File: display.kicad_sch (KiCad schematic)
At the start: 29 parts, among them Q1 HL2300, Q2 HL2300, Q3 HL2300, Q4 HL2300, Q5 HL2300, Q6 HL2300, Q7 HL2300, Q8 HL2300, U2 GS3911AG

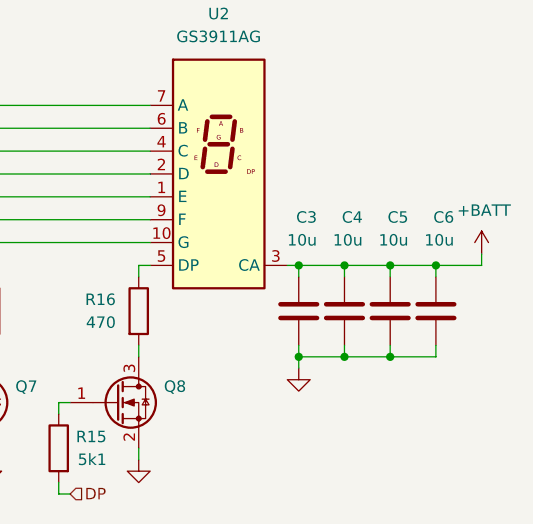
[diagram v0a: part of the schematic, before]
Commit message: schem: remove display extra decoupling caps
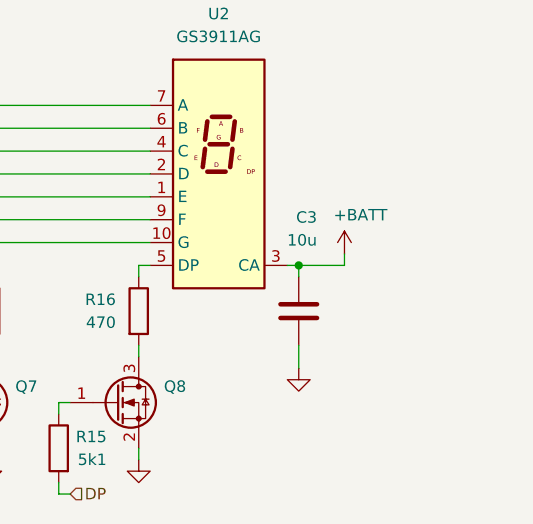
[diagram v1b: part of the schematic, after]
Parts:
- removed C4, C5, C6: 10u, Capacitor_SMD:C_0805_2012Metric, symbol Device:C

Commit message: pcb: add segment displays layout
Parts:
- added C4: 10u, Capacitor_SMD:C_0805_2012Metric, symbol Device:C
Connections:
- net +BATT: now also C4.1
- net GND: now also C4.2
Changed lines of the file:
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@@
 	)
 	(junction
+		(at 215.9 99.06)
+		(diameter 0)
+		(color 0 0 0 0)
+	)
+	(junction
 		(at 215.9 88.9)
 		(diameter 0)
 		(color 0 0 0 0)
 	)
+	(junction
+		(at 220.98 88.9)
+		(diameter 0)
+		(color 0 0 0 0)
+	)
 	(wire
 		(pts
@@
 	(wire
 		(pts
+			(xy 220.98 88.9) (xy 224.79 88.9)
+		)
+		(stroke
+			(width 0)
+			(type default)
+		)
+	)
+	(wire
+		(pts
 			(xy 199.39 83.82) (xy 165.1 83.82)
 		)
@@
 	(wire
 		(pts
+			(xy 220.98 88.9) (xy 220.98 90.17)
+		)
+		(stroke
+			(width 0)
+			(type default)
+		)
+	)
+	(wire
+		(pts
 			(xy 198.12 88.9) (xy 198.12 90.17)
 		)
@@
 	(wire
 		(pts
+			(xy 215.9 99.06) (xy 215.9 100.33)
+		)
+		(stroke
+			(width 0)
+			(type default)
+		)
+	)
+	(wire
+		(pts
+			(xy 220.98 99.06) (xy 220.98 97.79)
+		)
+		(stroke
+			(width 0)
+			(type default)
+		)
+	)
+	(wire
+		(pts
 			(xy 124.46 114.3) (xy 123.19 114.3)
 		)
@@
 	(wire
 		(pts
-			(xy 220.98 88.9) (xy 220.98 87.63)
+			(xy 224.79 88.9) (xy 224.79 87.63)
 		)
 		(stroke
@@
 	(wire
 		(pts
-			(xy 215.9 97.79) (xy 215.9 100.33)
+			(xy 215.9 97.79) (xy 215.9 99.06)
 		)
 		(stroke
@@
 	(wire
 		(pts
+			(xy 215.9 99.06) (xy 220.98 99.06)
+		)
+		(stroke
+			(width 0)
+			(type default)
+		)
+	)
+	(wire
+		(pts
 			(xy 181.61 109.22) (xy 181.61 110.49)
 		)
@@
 	)
 	(symbol
+		(lib_id "Device:C")
+		(at 220.98 93.98 0)
+		(unit 1)
+		(body_style 1)
+		(exclude_from_sim no)
+		(in_bom yes)
+		(on_board yes)
+		(in_pos_files yes)
+		(dnp no)
+		(property "Reference" "C4"
+			(at 223.012 83.566 0)
+			(show_name no)
+			(do_not_autoplace no)
+			(effects
+				(font
+					(size 1.27 1.27)
+				)
+				(justify right)
+			)
+		)
+		(property "Value" "10u"
+			(at 223.012 86.106 0)
+			(show_name no)
+			(do_not_autoplace no)
+			(effects
+				(font
+					(size 1.27 1.27)
+				)
+				(justify right)
+			)
+		)
+		(property "Footprint" "Capacitor_SMD:C_0805_2012Metric"
+			(at 221.9452 97.79 0)
+			(hide yes)
+			(show_name no)
+			(do_not_autoplace no)
+			(effects
+				(font
+					(size 1.27 1.27)
+				)
+			)
+		)
+		(property "Datasheet" ""
+			(at 220.98 93.98 0)
+			(hide yes)
+			(show_name no)
+			(do_not_autoplace no)
+			(effects
+				(font
+					(size 1.27 1.27)
+				)
+			)
+		)
+		(property "Description" "Unpolarized capacitor"
+			(at 220.98 93.98 0)
+			(hide yes)
+			(show_name no)
+			(do_not_autoplace no)
+			(effects
+				(font
+					(size 1.27 1.27)
+				)
+			)
+		)
+		(property "Basic" "Y"
+			(at 220.98 93.98 0)
+			(hide yes)
+			(show_name no)
+			(do_not_autoplace no)
+			(effects
+				(font
+					(size 1.27 1.27)
+				)
+			)
+		)
+		(property "JLCPCB Part #" "C440198"
+			(at 220.98 93.98 0)
+			(hide yes)
+			(show_name no)
+			(do_not_autoplace no)
+			(effects
+				(font
+					(size 1.27 1.27)
+				)
+			)
+		)
+		(property "Manufacturer" "Murata"
+			(at 220.98 93.98 0)
+			(hide yes)
+			(show_name no)
+			(do_not_autoplace no)
+			(effects
+				(font
+					(size 1.27 1.27)
+				)
+			)
+		)
+		(property "Manufacturer Part Number" "GRM21BR61H106KE43L"
+			(at 220.98 93.98 0)
+			(hide yes)
+			(show_name no)
+			(do_not_autoplace no)
+			(effects
+				(font
+					(size 1.27 1.27)
+				)
+			)
+		)
+		(pin "2"
+		)
+		(pin "1"
+		)
+		(instances
+			(project "dyb-segment-drv-1"
+				(path "/0d1f997b-7d97-47c3-85c1-1ce9346504d0/87467506-67cb-4d30-a7bb-1a482c54d28a"
+					(reference "C4")
+					(unit 1)
+				)
+				(path "/0d1f997b-7d97-47c3-85c1-1ce9346504d0/c18e9c5d-9680-45b1-9de5-05069c52084b"
+					(reference "C5")
+					(unit 1)
+				)
+			)
+		)
+	)
+	(symbol
 		(lib_id "Transistor_FET:DMN24H11DS")
 		(at 80.01 104.14 0)
@@
 	(symbol
 		(lib_id "power:+3V3")
-		(at 220.98 87.63 0)
+		(at 224.79 87.63 0)
 		(unit 1)
 		(body_style 1)
@@
 		(dnp no)
 		(property "Reference" "#PWR019"
-			(at 220.98 91.44 0)
+			(at 224.79 91.44 0)
 			(hide yes)
 			(show_name no)
@@
 		)
 		(property "Value" "+BATT"
-			(at 222.758 83.312 0)
+			(at 226.568 83.312 0)
 			(show_name no)
 			(do_not_autoplace no)
@@
 		)
 		(property "Footprint" ""
-			(at 220.98 87.63 0)
+			(at 224.79 87.63 0)
 			(hide yes)
 			(show_name no)
@@
 		)
 		(property "Datasheet" ""
-			(at 220.98 87.63 0)
+			(at 224.79 87.63 0)
 			(hide yes)
 			(show_name no)
@@
 		)
 		(property "Description" "Power symbol creates a global label with name \"+3V3\""
-			(at 220.98 87.63 0)
+			(at 224.79 87.63 0)
 			(hide yes)
 			(show_name no)
